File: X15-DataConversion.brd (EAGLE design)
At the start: 160 x 100 mm, 12 parts

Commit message: schematic actually finished now
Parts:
- added C6: 0.1uF, SparkFun-RF:0603
- added CAN_TRANCEIVER: MAX3058ASA+, CAN Tranceiver:MAX3058ASA+
- added CONNECTOR1: 3V3 -SWCLK-GND-SWDIO- NRST, CONN, Serial Wire Programming Headers:1X05
- added D3: Orange, SparkFun-LED:LED-0603
- added R5: 82, SparkFun-Resistors:0603
- added R6, R7: 120, SparkFun-Resistors:0603
- added STM: STM32F042K6T6, IC, STM32F042K6T6:STM32F042K6T6
- U$1: value STM32F042K6T6 -> DATACONV->BACKPLANE; device X15 Data Conversion:STM32F042K6T6 -> CONN, DataConversion-Backplane Connector- SAMTEC CLT-107-01-T-D:SAMTEC-CLT-107-01-X-D-DATACONV
- moved U$1 55.5 mm to (-24.1, -50.8)
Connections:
- new net CAN_H: CAN_TRANCEIVER.CANH, R6.2, R7.2, U$1.10
- new net CAN_L: CAN_TRANCEIVER.CANL, R6.1, R7.1, U$1.11
- new net N$1: D3.A, R5.1
- net 3.3V: now also C6.1, CAN_TRANCEIVER.VCC, CONNECTOR1.1, R5.2, STM.VDD, STM.VDDA, STM.VDDIO2, U$1.1; no longer U$1.VDD, U$1.VDDA, U$1.VDDIO2
- net ALERT1: now also STM.PB4, U$1.14; no longer U$1.PB4
- net ALERT2: now also STM.PB3, U$1.12; no longer U$1.PB3
- net C2_1: now also U$1.9
- net C2_2: now also U$1.7
- net CAN_RX: now also CAN_TRANCEIVER.RXD, STM.PA11; no longer U$1.PA11
- net CAN_TX: now also CAN_TRANCEIVER.TXD, STM.PA12; no longer U$1.PA12
- net CLK: now also STM.PA9, U$1.5; no longer U$1.PA9
- net DATA: now also STM.PA10, U$1.4; no longer U$1.PA10
- net GND: now also C6.2, CAN_TRANCEIVER.GND, CAN_TRANCEIVER.RS, CAN_TRANCEIVER.SHDN, CONNECTOR1.3, D3.C, STM.PB8-BOOT0, STM.VSS, STM.VSS1, U$1.2, U$1.3; no longer U$1.PB8-BOOT0, U$1.VSS, U$1.VSS1
- net LED: now also STM.PA15; no longer U$1.PA15
- net N$6: now also STM.PB1; no longer U$1.PB1
- net N$7: now also STM.PB0; no longer U$1.PB0
- net NRST: now also CONNECTOR1.5, STM.NRST, U$1.13; no longer U$1.NRST
- net SWCLK: now also CONNECTOR1.2, STM.PA14, U$1.8; no longer U$1.PA14
- net SWDIO: now also CONNECTOR1.4, STM.PA13, U$1.6; no longer U$1.PA13

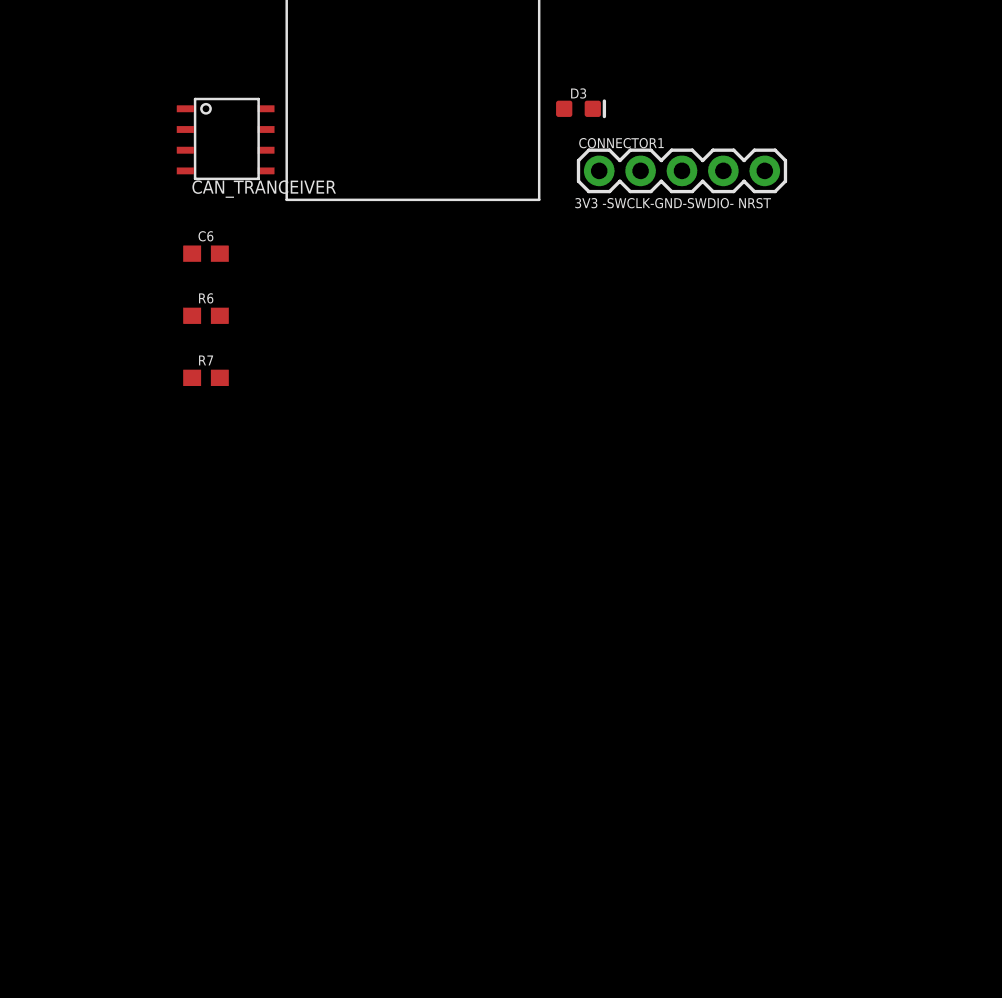
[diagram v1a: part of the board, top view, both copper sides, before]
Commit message: added oscillator
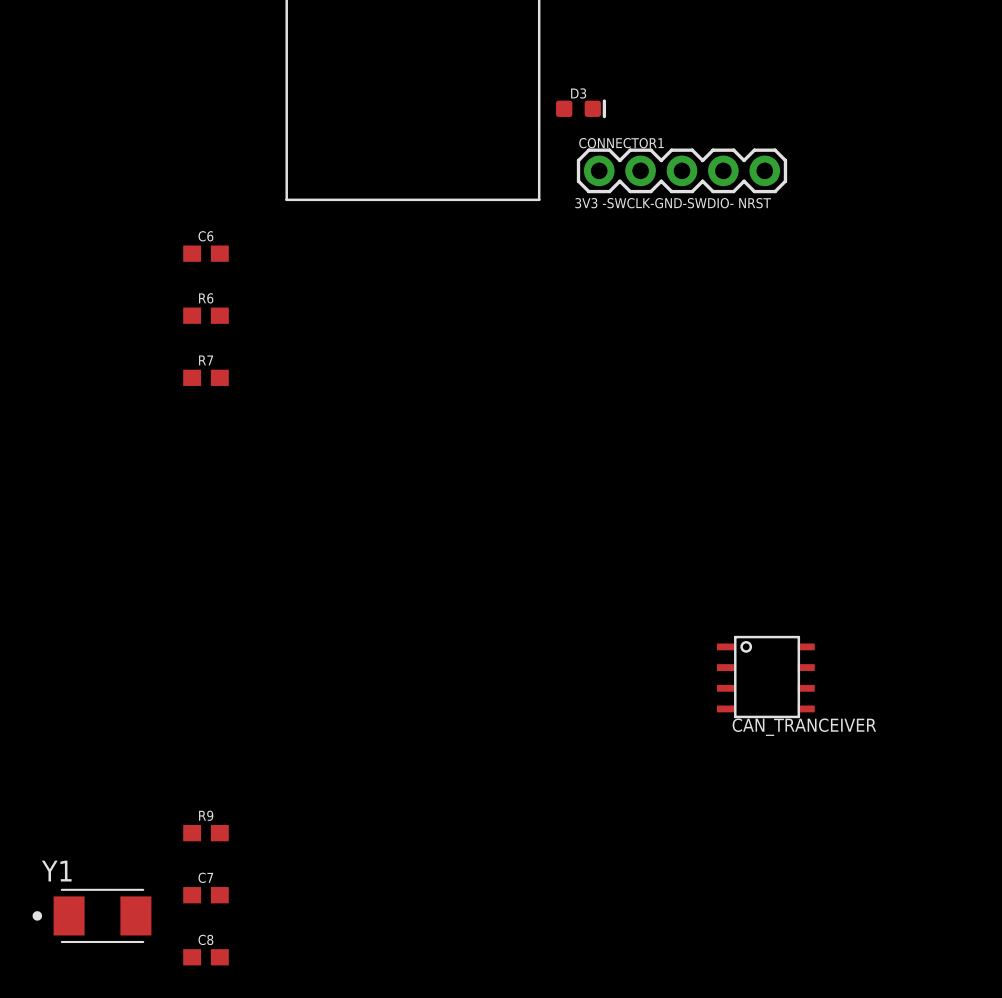
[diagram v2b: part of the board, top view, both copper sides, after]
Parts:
- added C7, C8: 18pF, SparkFun-RF:0603
- added R9: 1.5k, SparkFun-Resistors:0603
- added Y1: ECS-80-18-30-JGN-TR, ECS-80-18-30-JGN-TR:XTAL_ECS-80-18-30-JGN-TR
- CAN_TRANCEIVER: device CAN Tranceiver:MAX3058ASA+ -> IC,MAX3058ASA+:MAX3058ASA+
- moved CAN_TRANCEIVER 46.8 mm to (-4.95, -99.1)
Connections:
- new net N$3: C8.1, R9.1, Y1.2
- new net OSC_IN: C7.1, STM.PF0-OSC_IN, Y1.1
- new net OSC_OUT: R9.2, STM.PF1-OSC_OUT
- net GND: now also C7.2, C8.2
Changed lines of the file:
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@@
 <attribute name="NAME" x="-31.045" y="-47.483" size="1.016" layer="25"/>
 </element>
-<element name="CAN_TRANCEIVER" library="CAN Tranceiver" package="MAX3058ASA+" value="MAX3058ASA+" x="-38.1" y="-66.04" smashed="yes">
-<attribute name="NAME" x="-37.719" y="-71.247" size="0.8" layer="25"/>
-<attribute name="VALUE" x="-37.719" y="-65.278" size="0.8" layer="27"/>
+<element name="CAN_TRANCEIVER" library="IC,MAX3058ASA+" package="MAX3058ASA+" value="MAX3058ASA+" x="-4.95" y="-99.06" smashed="yes">
+<attribute name="NAME" x="-4.569" y="-104.267" size="0.8" layer="25"/>
+<attribute name="VALUE" x="-4.569" y="-98.298" size="0.8" layer="27"/>
 </element>
 <element name="C6" library="SparkFun-RF" package="0603" value="0.1uF" x="-36.83" y="-74.93" smashed="yes">
@@
 <attribute name="PROD_ID" value=" " x="-36.83" y="-82.55" size="1.778" layer="27" display="off"/>
 <attribute name="VALUE" x="-36.83" y="-83.312" size="0.6096" layer="27" font="vector" ratio="20" align="top-center"/>
+</element>
+<element name="R9" library="SparkFun-Resistors" package="0603" value="1.5k" x="-36.83" y="-110.49" smashed="yes">
+<attribute name="NAME" x="-36.83" y="-109.728" size="0.6096" layer="25" font="vector" ratio="20" align="bottom-center"/>
+<attribute name="PROD_ID" value=" " x="-35.56" y="-110.49" size="1.778" layer="27" display="off"/>
+<attribute name="VALUE" x="-36.83" y="-111.252" size="0.6096" layer="27" font="vector" ratio="20" align="top-center"/>
+</element>
+<element name="C7" library="SparkFun-RF" package="0603" value="18pF" x="-36.83" y="-114.3" smashed="yes">
+<attribute name="NAME" x="-36.83" y="-113.538" size="0.6096" layer="25" font="vector" ratio="20" align="bottom-center"/>
+<attribute name="PROD_ID" value="CAP-08604" x="-35.56" y="-114.3" size="1.778" layer="27" display="off"/>
+<attribute name="VALUE" x="-36.83" y="-115.062" size="0.6096" layer="27" font="vector" ratio="20" align="top-center"/>
+</element>
+<element name="C8" library="SparkFun-RF" package="0603" value="18pF" x="-36.83" y="-118.11" smashed="yes">
+<attribute name="NAME" x="-36.83" y="-117.348" size="0.6096" layer="25" font="vector" ratio="20" align="bottom-center"/>
+<attribute name="PROD_ID" value="CAP-08604" x="-35.56" y="-118.11" size="1.778" layer="27" display="off"/>
+<attribute name="VALUE" x="-36.83" y="-118.872" size="0.6096" layer="27" font="vector" ratio="20" align="top-center"/>
+</element>
+<element name="Y1" library="ECS-80-18-30-JGN-TR" package="XTAL_ECS-80-18-30-JGN-TR" value="ECS-80-18-30-JGN-TR" x="-43.18" y="-115.57" smashed="yes">
+<attribute name="DESCRIPTION" value=" 8 MHz ±20ppm Crystal 18pF 100 Ohms 2-SMD, No Lead " x="-43.18" y="-115.57" size="1.778" layer="27" display="off"/>
+<attribute name="DIGI-KEY_PART_NUMBER" value="XC2103TR-ND" x="-43.18" y="-115.57" size="1.778" layer="27" display="off"/>
+<attribute name="MF" value="ECS Inc." x="-43.18" y="-115.57" size="1.778" layer="27" display="off"/>
+<attribute name="MP" value="ECS-80-18-30-JGN-TR" x="-43.18" y="-115.57" size="1.778" layer="27" display="off"/>
+<attribute name="NAME" x="-46.89928125" y="-113.45771875" size="1.27743125" layer="25"/>
+<attribute name="PACKAGE" value="SMD-2 ECS International" x="-43.18" y="-115.57" size="1.778" layer="27" display="off"/>
+<attribute name="PURCHASE-URL" value="https://pricing.snapeda.com/search/part/ECS-80-18-30-JGN-TR/?ref=eda" x="-43.18" y="-115.57" size="1.778" layer="27" display="off"/>
+<attribute name="VALUE" x="-46.89308125" y="-119.0322" size="1.274490625" layer="27"/>
 </element>
 </elements>
@@
 <contactref element="CAN_TRANCEIVER" pad="SHDN"/>
 <contactref element="CAN_TRANCEIVER" pad="RS"/>
-<wire x1="-33.15" y1="-69.85" x2="-35.98" y2="-74.93" width="0" layer="19" extent="1-1"/>
-<wire x1="-33.15" y1="-66.04" x2="-33.15" y2="-69.85" width="0" layer="19" extent="1-1"/>
-<wire x1="-38.1" y1="-67.31" x2="-33.15" y2="-66.04" width="0" layer="19" extent="1-1"/>
-<wire x1="-30.13" y1="-51.8" x2="-33.15" y2="-66.04" width="0" layer="19" extent="1-1"/>
-<wire x1="-28.13" y1="-49.8" x2="-30.13" y2="-51.8" width="0" layer="19" extent="1-1"/>
-<wire x1="-13.093" y1="-66.04" x2="-33.15" y2="-66.04" width="0" layer="19" extent="1-1"/>
-<wire x1="-7.62" y1="-69.85" x2="-13.093" y2="-66.04" width="0" layer="19" extent="1-1"/>
+<contactref element="C7" pad="2"/>
+<contactref element="C8" pad="2"/>
+<wire x1="-35.98" y1="-114.3" x2="-35.98" y2="-118.11" width="0" layer="19" extent="1-1"/>
+<wire x1="-4.95" y1="-100.33" x2="-35.98" y2="-114.3" width="0" layer="19" extent="1-1"/>
+<wire x1="0" y1="-99.06" x2="-4.95" y2="-100.33" width="0" layer="19" extent="1-1"/>
+<wire x1="0" y1="-102.87" x2="0" y2="-99.06" width="0" layer="19" extent="1-1"/>
+<wire x1="-7.62" y1="-69.85" x2="0" y2="-99.06" width="0" layer="19" extent="1-1"/>
+<wire x1="-13.093" y1="-66.04" x2="-7.62" y2="-69.85" width="0" layer="19" extent="1-1"/>
 <wire x1="-1.45" y1="-54.61" x2="-13.093" y2="-66.04" width="0" layer="19" extent="1-1"/>
 <wire x1="-6.25" y1="-46.11" x2="-1.45" y2="-54.61" width="0" layer="19" extent="1-1"/>
@@
 <wire x1="-8.04" y1="-21.59" x2="-8.04" y2="-25.4" width="0" layer="19" extent="1-1"/>
 <wire x1="-8.04" y1="-6.35" x2="-8.04" y2="-21.59" width="0" layer="19" extent="1-1"/>
+<wire x1="-28.13" y1="-49.8" x2="-9.5" y2="-41.91" width="0" layer="19" extent="1-1"/>
+<wire x1="-30.13" y1="-51.8" x2="-28.13" y2="-49.8" width="0" layer="19" extent="1-1"/>
+<wire x1="-35.98" y1="-74.93" x2="-30.13" y2="-51.8" width="0" layer="19" extent="1-1"/>
 </signal>
 <signal name="NRST">
@@
 <contactref element="CAN_TRANCEIVER" pad="VCC"/>
 <contactref element="C6" pad="1"/>
-<wire x1="-38.1" y1="-68.58" x2="-37.68" y2="-74.93" width="0" layer="19" extent="1-1"/>
-<wire x1="-30.13" y1="-49.8" x2="-38.1" y2="-68.58" width="0" layer="19" extent="1-1"/>
-<wire x1="-13.12" y1="-58.42" x2="-30.13" y2="-49.8" width="0" layer="19" extent="1-1"/>
+<wire x1="-12.7" y1="-69.85" x2="-37.68" y2="-74.93" width="0" layer="19" extent="1-1"/>
+<wire x1="-13.12" y1="-58.42" x2="-12.7" y2="-69.85" width="0" layer="19" extent="1-1"/>
 <wire x1="-8.5" y1="-50.76" x2="-13.12" y2="-58.42" width="0" layer="19" extent="1-1"/>
 <wire x1="-8.5" y1="-47.56" x2="-8.5" y2="-50.76" width="0" layer="19" extent="1-1"/>
 <wire x1="0" y1="-53.16" x2="-8.5" y2="-50.76" width="0" layer="19" extent="1-1"/>
-<wire x1="-12.7" y1="-69.85" x2="-13.12" y2="-58.42" width="0" layer="19" extent="1-1"/>
 <wire x1="-9.74" y1="-33.02" x2="-8.5" y2="-47.56" width="0" layer="19" extent="1-1"/>
 <wire x1="-9.74" y1="-29.21" x2="-9.74" y2="-33.02" width="0" layer="19" extent="1-1"/>
 <wire x1="-9.74" y1="-25.4" x2="-9.74" y2="-29.21" width="0" layer="19" extent="1-1"/>
 <wire x1="-9.74" y1="-21.59" x2="-9.74" y2="-25.4" width="0" layer="19" extent="1-1"/>
+<wire x1="-30.13" y1="-49.8" x2="-13.12" y2="-58.42" width="0" layer="19" extent="1-1"/>
 <wire x1="-8.04" y1="-2.54" x2="-9.74" y2="-21.59" width="0" layer="19" extent="1-1"/>
+<wire x1="-4.95" y1="-101.6" x2="-12.7" y2="-69.85" width="0" layer="19" extent="1-1"/>
 </signal>
 <signal name="ALERT1">
@@
 <contactref element="STM" pad="PA12"/>
 <contactref element="CAN_TRANCEIVER" pad="TXD"/>
-<wire x1="0" y1="-49.16" x2="-38.1" y2="-66.04" width="0" layer="19" extent="1-1"/>
+<wire x1="0" y1="-49.16" x2="-4.95" y2="-99.06" width="0" layer="19" extent="1-1"/>
 </signal>
 <signal name="CAN_RX">
 <contactref element="STM" pad="PA11"/>
 <contactref element="CAN_TRANCEIVER" pad="RXD"/>
-<wire x1="0" y1="-49.96" x2="-38.1" y2="-69.85" width="0" layer="19" extent="1-1"/>
+<wire x1="0" y1="-49.96" x2="-4.95" y2="-102.87" width="0" layer="19" extent="1-1"/>
 </signal>
 <signal name="DATA">
@@
 <contactref element="R7" pad="1"/>
 <wire x1="-37.68" y1="-78.74" x2="-37.68" y2="-82.55" width="0" layer="19" extent="1-1"/>
-<wire x1="-33.15" y1="-68.58" x2="-37.68" y2="-78.74" width="0" layer="19" extent="1-1"/>
-<wire x1="-20.13" y1="-49.8" x2="-33.15" y2="-68.58" width="0" layer="19" extent="1-1"/>
+<wire x1="-20.13" y1="-49.8" x2="-37.68" y2="-78.74" width="0" layer="19" extent="1-1"/>
+<wire x1="0" y1="-101.6" x2="-37.68" y2="-82.55" width="0" layer="19" extent="1-1"/>
 </signal>
 <signal name="CAN_H">
@@
 <contactref element="CAN_TRANCEIVER" pad="CANH"/>
 <wire x1="-35.98" y1="-78.74" x2="-35.98" y2="-82.55" width="0" layer="19" extent="1-1"/>
-<wire x1="-33.15" y1="-67.31" x2="-35.98" y2="-78.74" width="0" layer="19" extent="1-1"/>
-<wire x1="-22.13" y1="-51.8" x2="-33.15" y2="-67.31" width="0" layer="19" extent="1-1"/>
+<wire x1="-22.13" y1="-51.8" x2="-35.98" y2="-78.74" width="0" layer="19" extent="1-1"/>
+<wire x1="0" y1="-100.33" x2="-35.98" y2="-82.55" width="0" layer="19" extent="1-1"/>
+</signal>
+<signal name="OSC_IN">
+<contactref element="STM" pad="PF0-OSC_IN"/>
+<contactref element="C7" pad="1"/>
+<contactref element="Y1" pad="1"/>
+<wire x1="-37.68" y1="-114.3" x2="-45.23" y2="-115.57" width="0" layer="19" extent="1-1"/>
+<wire x1="-8.5" y1="-48.36" x2="-37.68" y2="-114.3" width="0" layer="19" extent="1-1"/>
+</signal>
+<signal name="OSC_OUT">
+<contactref element="STM" pad="PF1-OSC_OUT"/>
+<contactref element="R9" pad="2"/>
+<wire x1="-8.5" y1="-49.16" x2="-35.98" y2="-110.49" width="0" layer="19" extent="1-1"/>
+</signal>
+<signal name="N$3">
+<contactref element="C8" pad="1"/>
+<contactref element="R9" pad="1"/>
+<contactref element="Y1" pad="2"/>
+<wire x1="-37.68" y1="-118.11" x2="-41.13" y2="-115.57" width="0" layer="19" extent="1-1"/>
+<wire x1="-37.68" y1="-110.49" x2="-41.13" y2="-115.57" width="0" layer="19" extent="1-1"/>
 </signal>
 </signals>

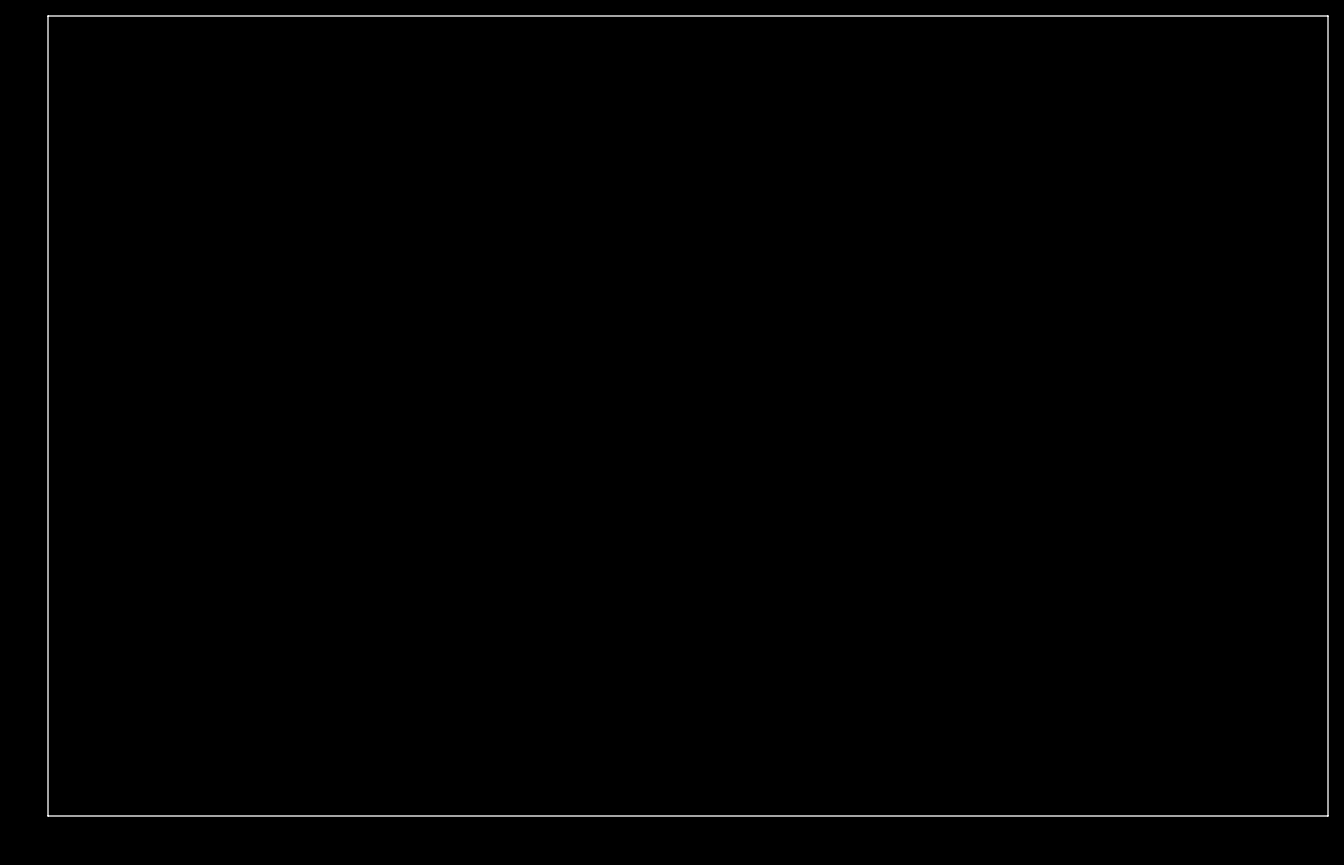
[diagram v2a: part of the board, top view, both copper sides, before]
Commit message: board dimensions
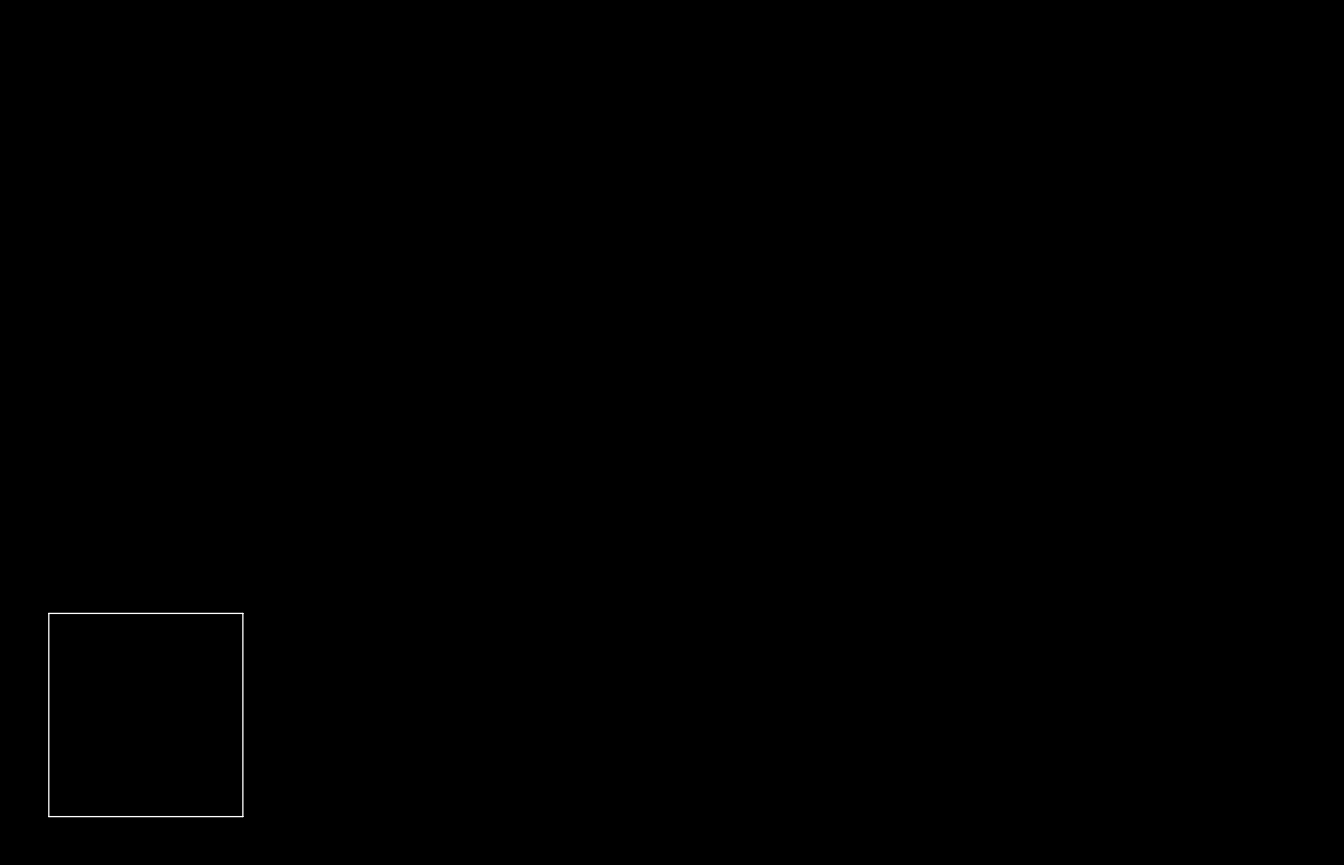
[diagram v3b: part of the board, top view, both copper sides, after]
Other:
- board size 160 x 100 mm -> 24.3 x 25.4 mm
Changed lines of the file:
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@@
 <setting verticaltext="up"/>
 </settings>
-<grid distance="50" unitdist="mil" unit="mil" style="lines" multiple="1" display="no" altdistance="5" altunitdist="mil" altunit="mil"/>
+<grid distance="1" unitdist="mil" unit="mil" style="lines" multiple="1" display="no" altdistance="5" altunitdist="mil" altunit="mil"/>
 <layers>
 <layer number="1" name="Top" color="4" fill="1" visible="yes" active="yes"/>
@@
 <board>
 <plain>
-<wire x1="0" y1="0" x2="160" y2="0" width="0" layer="20"/>
-<wire x1="160" y1="0" x2="160" y2="100" width="0" layer="20"/>
-<wire x1="160" y1="100" x2="0" y2="100" width="0" layer="20"/>
-<wire x1="0" y1="100" x2="0" y2="0" width="0" layer="20"/>
+<wire x1="0.1016" y1="-0.0762" x2="24.3586" y2="-0.0762" width="0" layer="20"/>
+<wire x1="24.3586" y1="-0.0762" x2="24.3586" y2="25.3238" width="0" layer="20"/>
+<wire x1="24.3586" y1="25.3238" x2="0.1016" y2="25.3238" width="0" layer="20"/>
+<wire x1="0.1016" y1="25.3238" x2="0.1016" y2="-0.0762" width="0" layer="20"/>
 </plain>
 <attributes>
